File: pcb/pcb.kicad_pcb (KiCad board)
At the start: 2 copper layers, 79 x 95 mm, 28 parts, among them J1 Screw_Terminal_01x02, J2 Screw_Terminal_01x04, J3 Screw_Terminal_01x04, Q1 2N7000, Q2 2N7000, Q3 2N7000

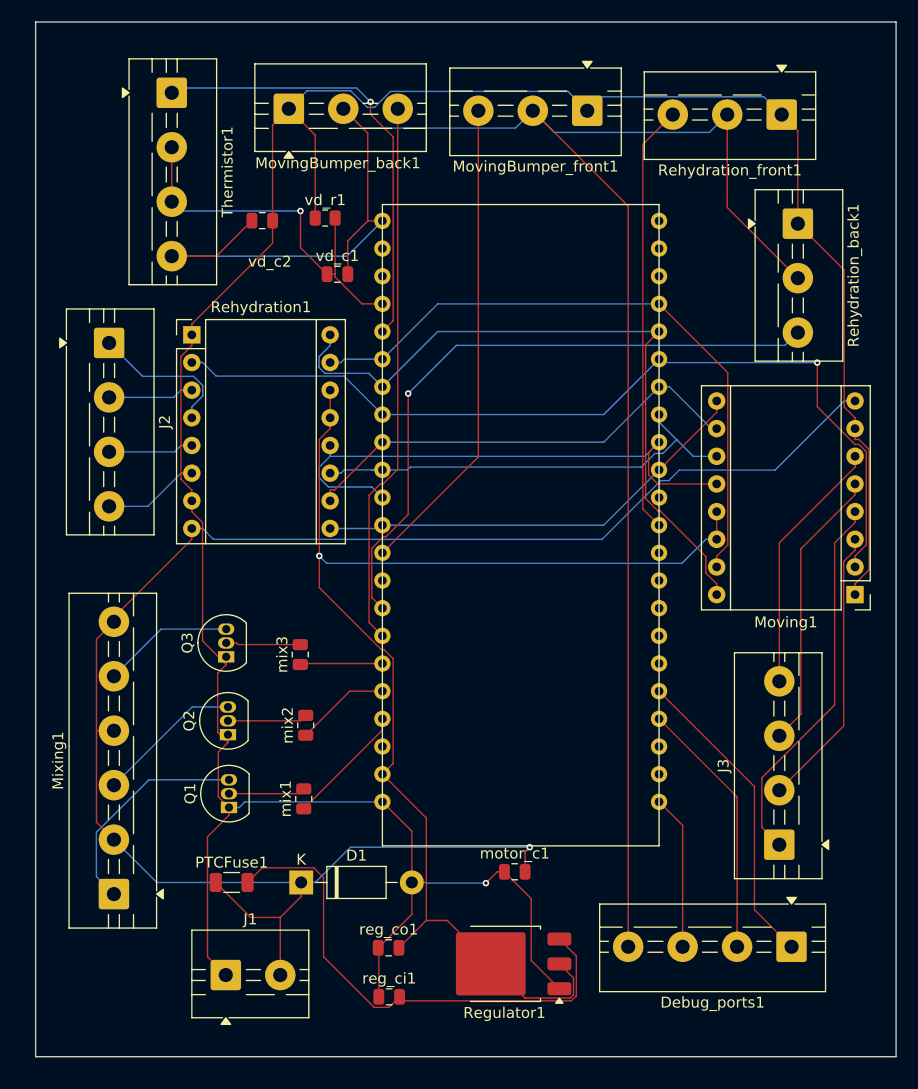
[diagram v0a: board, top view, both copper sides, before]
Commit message: added text to pcb to show on gerber files
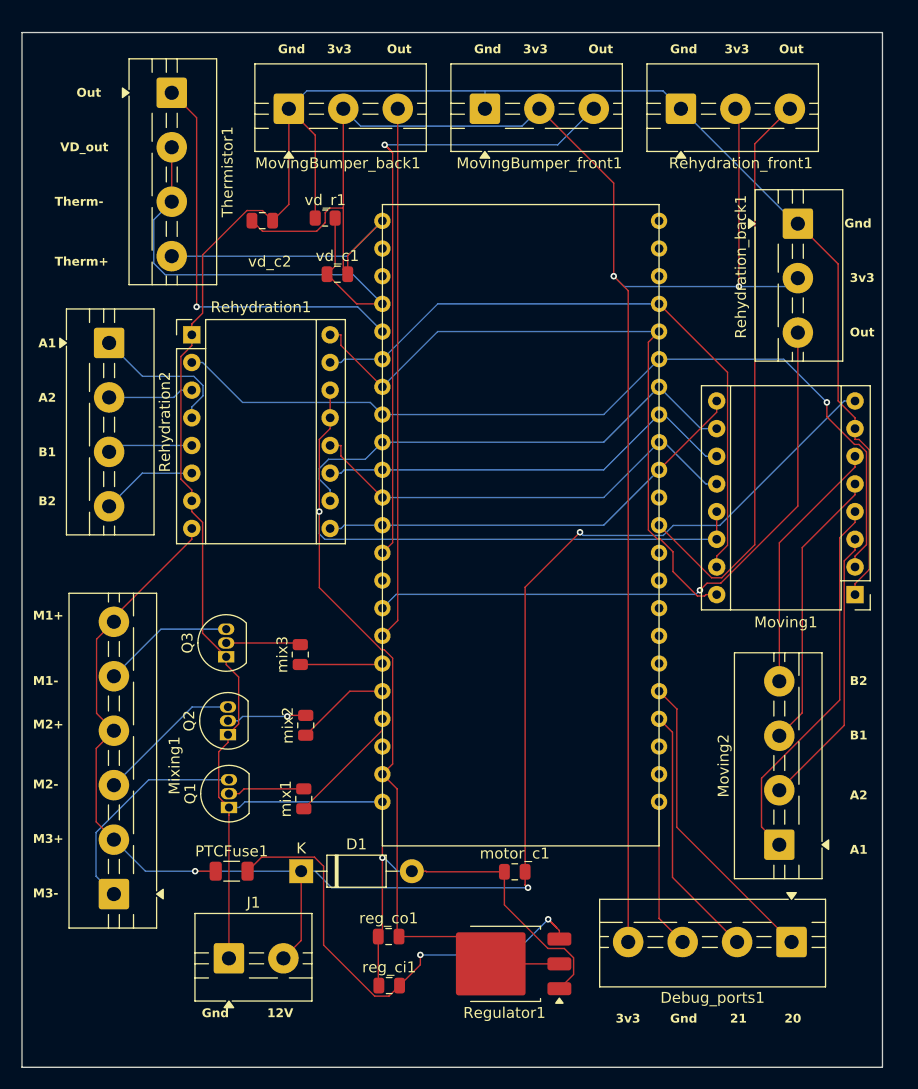
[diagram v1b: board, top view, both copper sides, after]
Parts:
- moved MovingBumper_front1 9.40 mm to (138.0, 57.5), turned to 0 degrees
- moved Rehydration_front1 9.27 mm to (156.0, 57.5), turned to 0 degrees
- moved J1 1.56 mm to (114.5, 135.5)
- moved D1 1.03 mm to (121.1, 127.5)
- moved PTCFuse1 1.03 mm to (114.8, 127.5)
- moved reg_ci1 1.03 mm to (129.2, 138.0)
- moved reg_co1 1.03 mm to (129.2, 133.5)
- moved Debug_ports1 0.44 mm to (166.2, 134.0)
- renumbered J3 to Moving2, J2 to Rehydration2
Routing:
- net /B_F: track 44.2 -> 62.6 mm, vias 0 -> 1
- net /R_F: track 39.5 -> 53.4 mm
- net Net-(D1-K): track 163.6 -> 152.2 mm, vias 1 -> 3
- net /VD_o: track 35.5 -> 45.5 mm, vias 1 -> 0
- net /M2: track 50.7 -> 41.7 mm
- net /5V: track 117.9 -> 111.6 mm
- net Net-(D1-A): track 254.5 -> 249.0 mm
- net /Heating_pwm: track 41.3 -> 38.6 mm
- net /M0: track 42.0 -> 44.6 mm
- net /M1: track 41.3 -> 39.3 mm
- net Net-(Debug_ports1-Pin_4): track 183.9 -> 185.7 mm, vias 0 -> 2
- net /R_B: track 59.7 -> 58.0 mm
- net /DIR: track 65.0 -> 63.4 mm
- net /FLT: track 82.9 -> 81.3 mm
- net /B_B: track 50.1 -> 49.0 mm
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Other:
- board text added: "12V"
- board text added: "20"
- board text added: "21"
- board text added: "3v3"
- board text added: "A1"
- board text added: "A2"
- board text added: "B1"
- board text added: "B2"
- board text added: "Gnd"
- board text added: "M1+"
- board text added: "M1-"
- board text added: "M2+"
- board text added: "M2-"
- board text added: "M3+"
- board text added: "M3-"
- board text added: "Out"
- board text added: "Therm+"
- board text added: "Therm-"
- board text added: "VD_out"
